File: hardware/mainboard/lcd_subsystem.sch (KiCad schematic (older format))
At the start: 1 part, among them J2 WP7B-S040VA1-R6000

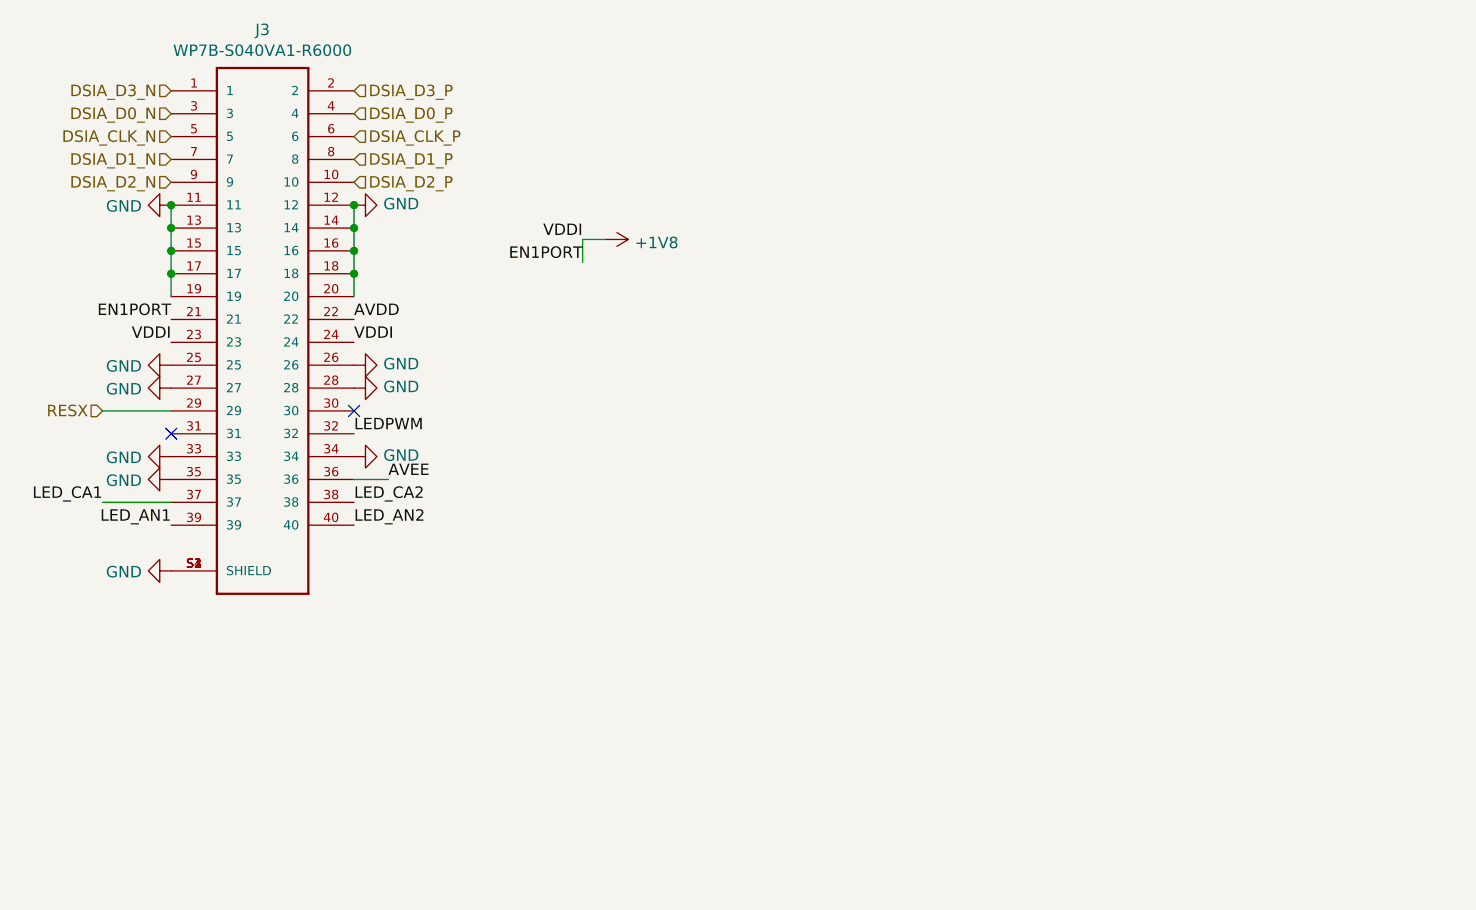
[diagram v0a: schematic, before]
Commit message: displays done, sd card and camera is left
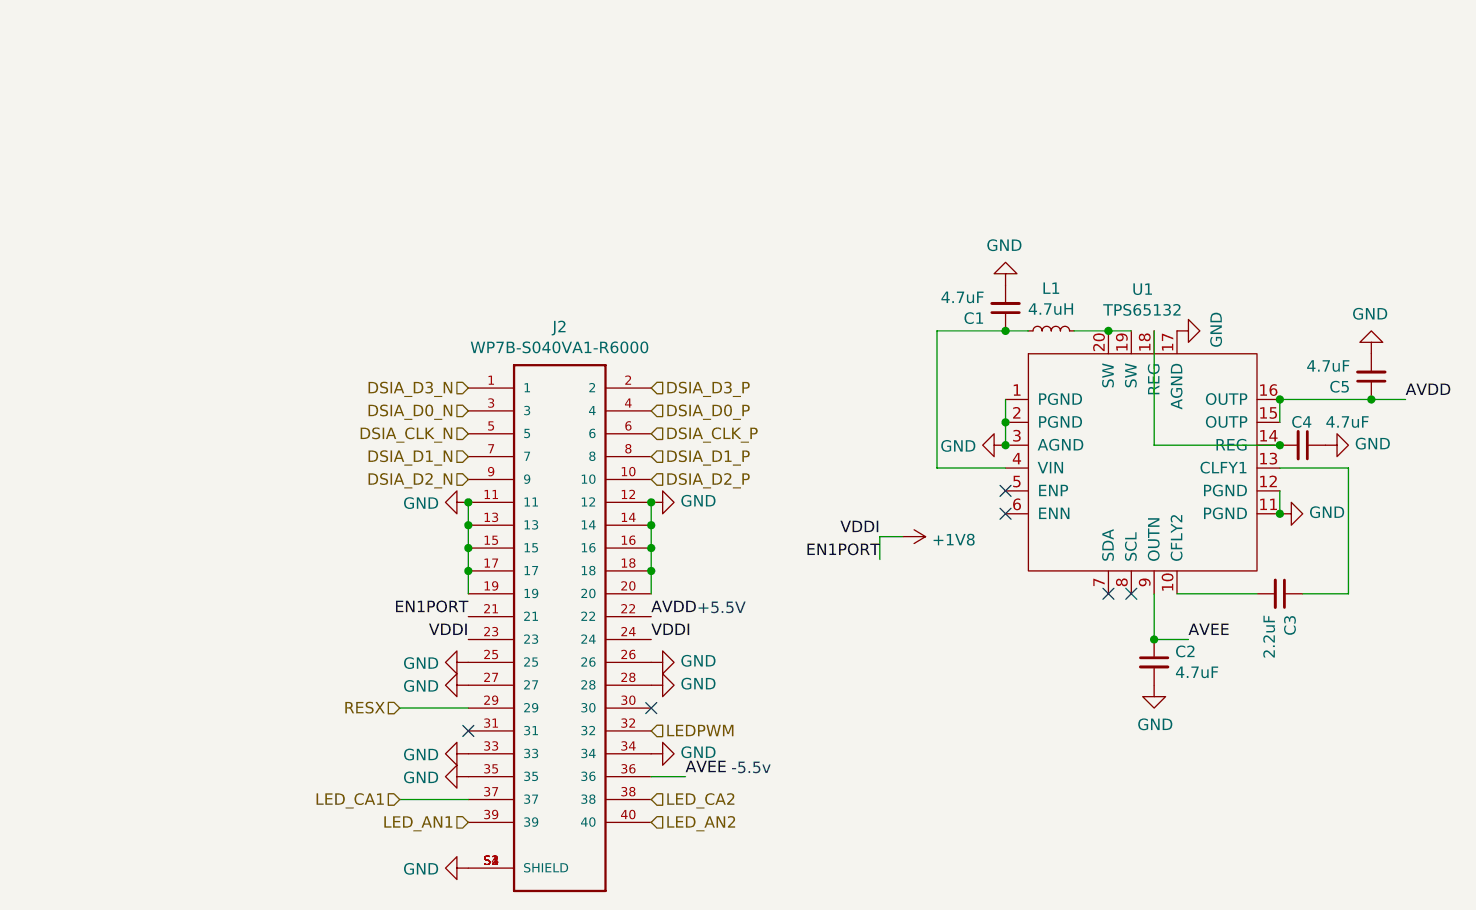
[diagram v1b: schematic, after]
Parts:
- added C1, C2, C4, C5: 4.7uF, symbol Device:C_Small
- added C3: 2.2uF, symbol Device:C_Small
- added L1: 4.7uH, symbol Device:L_Small
- added U1: TPS65132, symbol mainboard:TPS65132
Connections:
- net AVDD: now also C5.1, U1.15 (OUTP), U1.16 (OUTP)
- net AVEE: now also C2.1, U1.9 (OUTN)
- net GND: now also C1.2, C2.2, C4.1, C5.2, U1.1 (PGND), U1.11 (PGND), U1.12 (PGND), U1.17 (AGND), U1.2 (PGND), U1.3 (AGND)
- new net: C3.2, U1.10 (CFLY2)
- new net: C3.1, U1.13 (CLFY1)
- new net: C4.2, U1.14 (REG), U1.18 (REG)
- new net: L1.2, U1.19 (SW), U1.20 (SW)
- new net: C1.1, L1.1, U1.4 (VIN)
- no-connect marks 2 -> 6
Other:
- note added: "+5.5V"
- note added: "-5.5v\n"
- moved on the sheet: J2

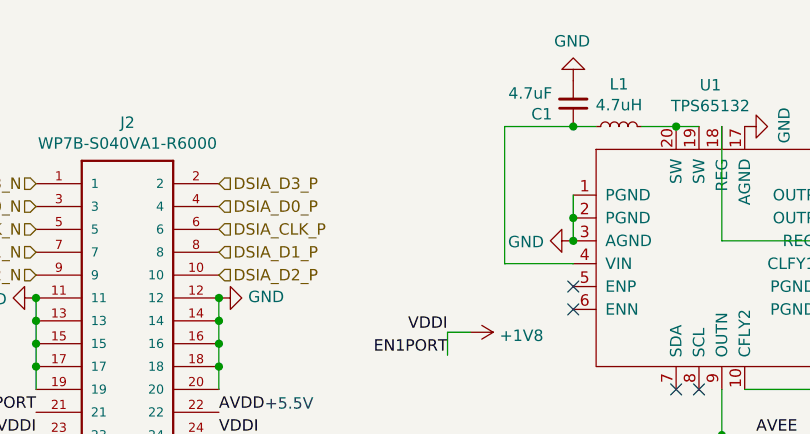
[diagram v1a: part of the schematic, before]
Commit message: finished camera, sd, imu, power supplies, might be done with schematic
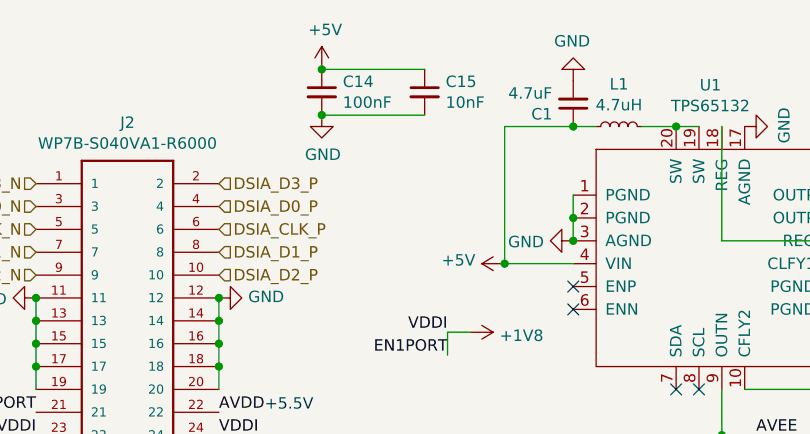
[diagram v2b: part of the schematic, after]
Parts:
- added C14: 100nF, symbol Device:C_Small
- added C15: 10nF, symbol Device:C_Small
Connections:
- net GND: now also C14.2, C15.2
- net +5V: now reaches C1.1, L1.1, U1.4 (VIN)
- net +5V: now also C14.1, C15.1
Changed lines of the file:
@@
 $Descr A4 11693 8268
 encoding utf-8
-Sheet 4 4
+Sheet 2 3
 Title ""
 Date ""
@@
 AR Path="/5F89AA7A/5FA221C8" Ref="J3"  Part="1"
 AR Path="/5FA3B5FC/5FA221C8" Ref="J?"  Part="1"
-AR Path="/5FA75E62/5FA221C8" Ref="J?"  Part="1"
-F 0 "J?" H 4750 5717 50  0000 C CNN
+AR Path="/5FA75E62/5FA221C8" Ref="J6"  Part="1"
+F 0 "J2" H 4750 5717 50  0000 C CNN
 F 1 "WP7B-S040VA1-R6000" H 4750 5626 50  0000 C CNN
 F 2 "JAE_WP7B-S040VA1-R6000" H 4750 4450 50  0001 L BNN
@@
 AR Path="/5F89AA7A/5F8F28BE" Ref="C7"  Part="1"
 AR Path="/5FA3B5FC/5F8F28BE" Ref="C?"  Part="1"
-AR Path="/5FA75E62/5F8F28BE" Ref="C?"  Part="1"
-F 0 "C?" H 7442 4696 50  0000 L CNN
+AR Path="/5FA75E62/5F8F28BE" Ref="C19"  Part="1"
+F 0 "C2" H 7442 4696 50  0000 L CNN
 F 1 "4.7uF" H 7442 4605 50  0000 L CNN
 F 2 "" H 7350 4650 50  0001 C CNN
@@
 AR Path="/5F89AA7A/5F8D1308" Ref="C10"  Part="1"
 AR Path="/5FA3B5FC/5F8D1308" Ref="C?"  Part="1"
-AR Path="/5FA75E62/5F8D1308" Ref="C?"  Part="1"
-F 0 "C?" H 8392 3446 50  0000 L CNN
+AR Path="/5FA75E62/5F8D1308" Ref="C22"  Part="1"
+F 0 "C5" H 8392 3446 50  0000 L CNN
 F 1 "4.7uF" H 8392 3355 50  0000 L CNN
 F 2 "" H 8300 3400 50  0001 C CNN
@@
 AR Path="/5F89AA7A/5F8FE2CF" Ref="C9"  Part="1"
 AR Path="/5FA3B5FC/5F8FE2CF" Ref="C?"  Part="1"
-AR Path="/5FA75E62/5F8FE2CF" Ref="C?"  Part="1"
-F 0 "C?" V 7900 3650 50  0000 L CNN
+AR Path="/5FA75E62/5F8FE2CF" Ref="C21"  Part="1"
+F 0 "C4" V 7900 3650 50  0000 L CNN
 F 1 "4.7uF" V 7900 3800 50  0000 L CNN
 F 2 "" H 8000 3700 50  0001 C CNN
@@
 AR Path="/5F89AA7A/5F901A08" Ref="C8"  Part="1"
 AR Path="/5FA3B5FC/5F901A08" Ref="C?"  Part="1"
-AR Path="/5FA75E62/5F901A08" Ref="C?"  Part="1"
-F 0 "C?" H 7992 4396 50  0000 L CNN
+AR Path="/5FA75E62/5F901A08" Ref="C20"  Part="1"
+F 0 "C3" H 7992 4396 50  0000 L CNN
 F 1 "2.2uF" H 7992 4305 50  0000 L CNN
 F 2 "" H 7900 4350 50  0001 C CNN
@@
 AR Path="/5F89AA7A/5F908EBB" Ref="L2"  Part="1"
 AR Path="/5FA3B5FC/5F908EBB" Ref="L?"  Part="1"
-AR Path="/5FA75E62/5F908EBB" Ref="L?"  Part="1"
-F 0 "L?" V 7085 3200 50  0000 C CNN
+AR Path="/5FA75E62/5F908EBB" Ref="L2"  Part="1"
+F 0 "L1" V 7085 3200 50  0000 C CNN
 F 1 "4.7uH" V 6994 3200 50  0000 C CNN
 F 2 "" H 6900 3200 50  0001 C CNN
@@
 AR Path="/5F89AA7A/5F90F3A3" Ref="C6"  Part="1"
 AR Path="/5FA3B5FC/5F90F3A3" Ref="C?"  Part="1"
-AR Path="/5FA75E62/5F90F3A3" Ref="C?"  Part="1"
-F 0 "C?" H 6792 3146 50  0000 L CNN
+AR Path="/5FA75E62/5F90F3A3" Ref="C18"  Part="1"
+F 0 "C1" H 6792 3146 50  0000 L CNN
 F 1 "4.7uF" H 6792 3055 50  0000 L CNN
 F 2 "" H 6700 3100 50  0001 C CNN
@@
 AR Path="/5F89AA7A/5F8CA6D9" Ref="U2"  Part="1"
 AR Path="/5FA3B5FC/5F8CA6D9" Ref="U?"  Part="1"
-AR Path="/5FA75E62/5F8CA6D9" Ref="U?"  Part="1"
-F 0 "U?" H 7300 4381 50  0000 C CNN
+AR Path="/5FA75E62/5F8CA6D9" Ref="U4"  Part="1"
+F 0 "U1" H 7300 4381 50  0000 C CNN
 F 1 "TPS65132" H 7300 4290 50  0000 C CNN
 F 2 "" H 7300 3650 50  0001 C CNN
@@
 Text HLabel 5150 4950 2    50   Input ~ 0
 LEDPWM
+$Comp
+L power:+5V #PWR0262
+U 1 1 6021D52E
+P 6400 3800
+AR Path="/5F86493C/6021D52E" Ref="#PWR0262"  Part="1"
+AR Path="/5FA75E62/6021D52E" Ref="#PWR0265"  Part="1"
+F 0 "#PWR0265" H 6400 3650 50  0001 C CNN
+F 1 "+5V" V 6415 3928 50  0000 L CNN
+F 2 "" H 6400 3800 50  0001 C CNN
+F 3 "" H 6400 3800 50  0001 C CNN
+	1    6400 3800
+	0    -1   -1   0
+$EndComp
+Connection ~ 6400 3800
+$Comp
+L Device:C_Small C14
+U 1 1 6021F152
+P 5600 3050
+AR Path="/5F86493C/6021F152" Ref="C14"  Part="1"
+AR Path="/5FA75E62/6021F152" Ref="C16"  Part="1"
+F 0 "C14" H 5692 3096 50  0000 L CNN
+F 1 "100nF" H 5692 3005 50  0000 L CNN
+F 2 "" H 5600 3050 50  0001 C CNN
+F 3 "~" H 5600 3050 50  0001 C CNN
+	1    5600 3050
+	1    0    0    -1
+$EndComp
+$Comp
+L power:GND #PWR0263
+U 1 1 6021FA8C
+P 5600 3150
+AR Path="/5F86493C/6021FA8C" Ref="#PWR0263"  Part="1"
+AR Path="/5FA75E62/6021FA8C" Ref="#PWR0266"  Part="1"
+F 0 "#PWR0266" H 5600 2900 50  0001 C CNN
+F 1 "GND" H 5605 2977 50  0000 C CNN
+F 2 "" H 5600 3150 50  0001 C CNN
+F 3 "" H 5600 3150 50  0001 C CNN
+	1    5600 3150
+	1    0    0    -1
+$EndComp
+$Comp
+L power:+5V #PWR0264
+U 1 1 6021FEAB
+P 5600 2950
+AR Path="/5F86493C/6021FEAB" Ref="#PWR0264"  Part="1"
+AR Path="/5FA75E62/6021FEAB" Ref="#PWR0267"  Part="1"
+F 0 "#PWR0267" H 5600 2800 50  0001 C CNN
+F 1 "+5V" H 5615 3123 50  0000 C CNN
+F 2 "" H 5600 2950 50  0001 C CNN
+F 3 "" H 5600 2950 50  0001 C CNN
+	1    5600 2950
+	1    0    0    -1
+$EndComp
+$Comp
+L Device:C_Small C15
+U 1 1 602249E9
+P 6050 3050
+AR Path="/5F86493C/602249E9" Ref="C15"  Part="1"
+AR Path="/5FA75E62/602249E9" Ref="C17"  Part="1"
+F 0 "C15" H 6142 3096 50  0000 L CNN
+F 1 "10nF" H 6142 3005 50  0000 L CNN
+F 2 "" H 6050 3050 50  0001 C CNN
+F 3 "~" H 6050 3050 50  0001 C CNN
+	1    6050 3050
+	1    0    0    -1
+$EndComp
+Wire Wire Line
+	5600 2950 6050 2950
+Connection ~ 5600 2950
+Wire Wire Line
+	5600 3150 6050 3150
+Connection ~ 5600 3150
 $EndSCHEMATC
